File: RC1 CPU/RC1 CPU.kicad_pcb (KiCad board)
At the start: 2 copper layers, 99.1 x 99.1 mm, 43 parts, among them J1 Expansion, J2 RC1_UI_Port, J3 BARREL_JACK, M1 Mounting, M2 Mounting, M3 Mounting, M4 Mounting, U1 WD65C02, U2 HM62256BLP-7, U3 28C256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

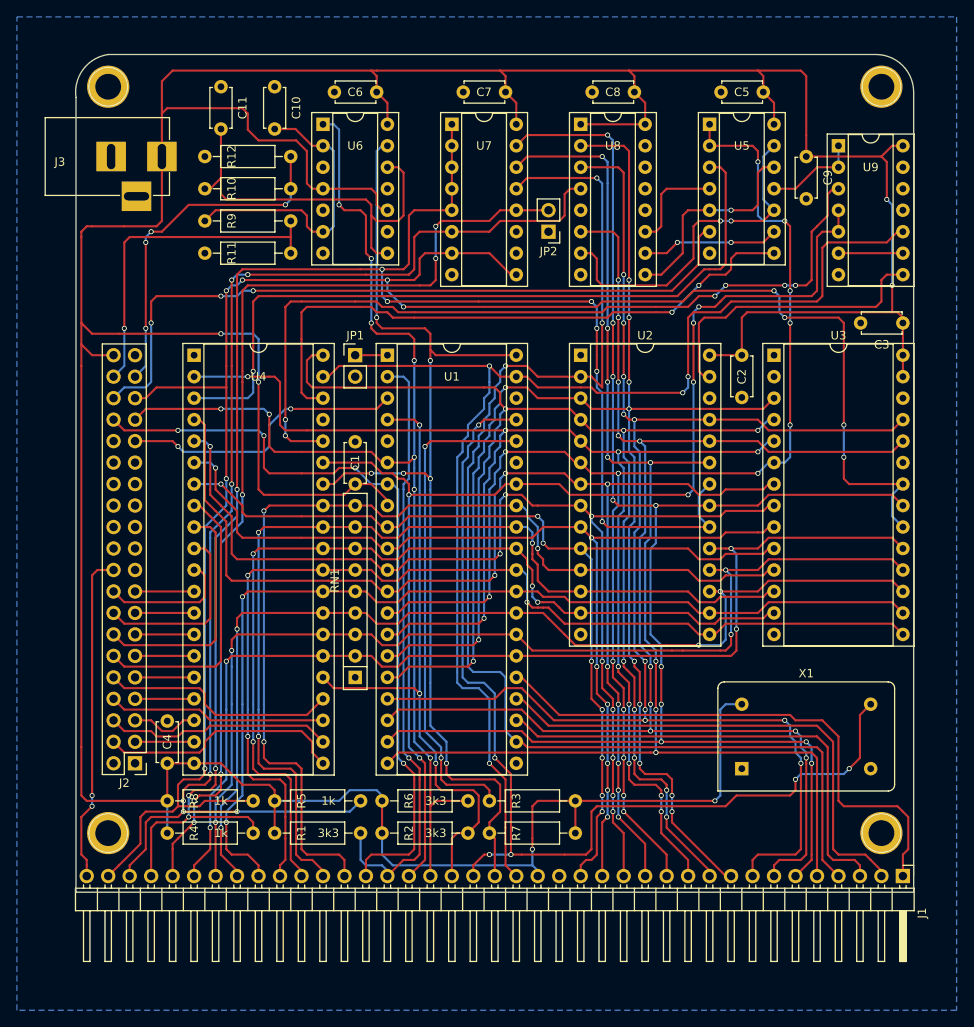
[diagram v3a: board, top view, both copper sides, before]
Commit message: Tweaked silkscreens and exported gerbers for CPU/UI
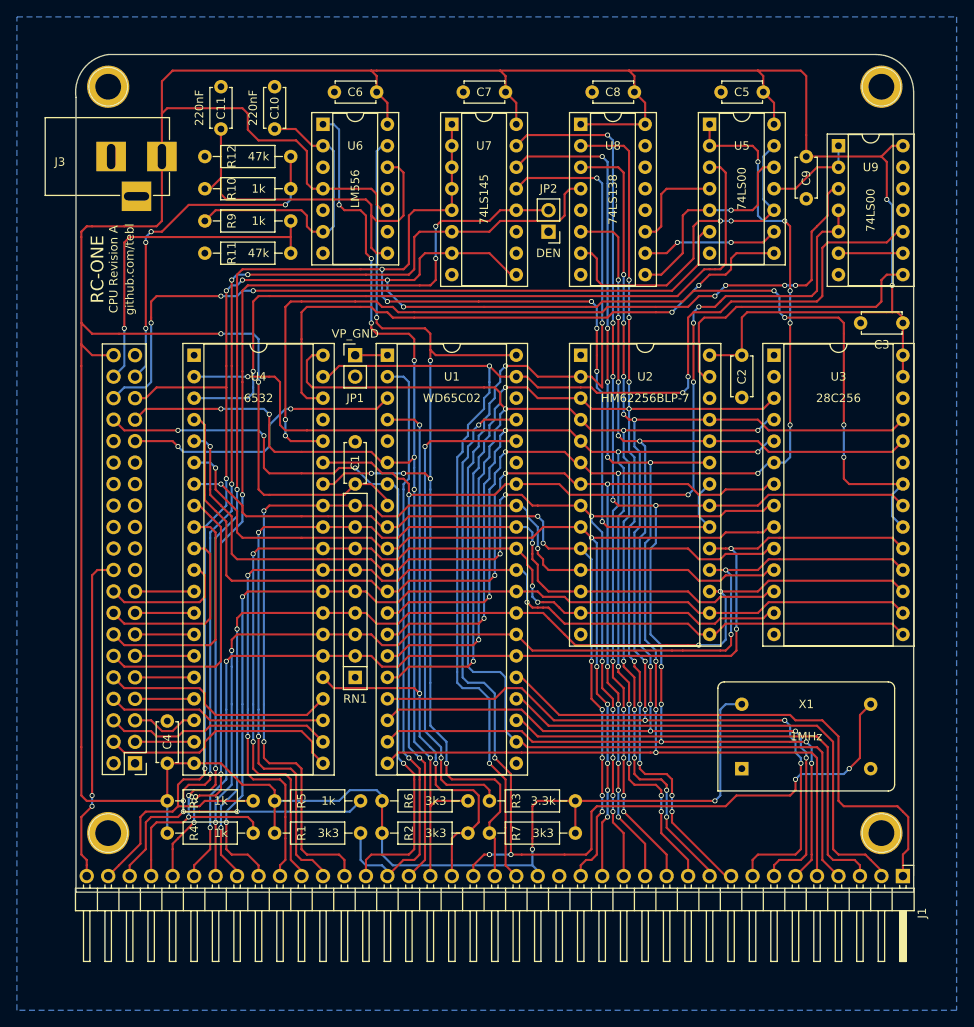
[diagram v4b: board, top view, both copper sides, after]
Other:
- board text added: "CPU Revision A"
- board text added: "RC-ONE"
- board text added: "github.com/tebl"
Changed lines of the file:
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@@
     (area 100.209871 48.184999 199.465001 147.395001)
     (thickness 1.6)
-    (drawings 6)
+    (drawings 9)
     (tracks 1946)
     (zones 0)
@@
     (descr "Through hole straight pin header, 2x20, 2.54mm pitch, double rows")
     (tags "Through hole pin header THT 2x20 2.54mm double row")
-    (fp_text reference J2 (at 1.27 -2.33 180) (layer F.SilkS)
-      (effects (font (size 1 1) (thickness 0.15)))
-    )
-    (fp_text value RC1_UI_Port (at 1.27 50.59 180) (layer F.Fab)
+    (fp_text reference J2 (at 1.27 -2.54 180) (layer F.Fab)
+      (effects (font (size 1 1) (thickness 0.15)))
+    )
+    (fp_text value RC1_UI_Port (at 1.27 50.8 180) (layer F.Fab)
       (effects (font (size 1 1) (thickness 0.15)))
     )
@@
     (descr "C, Disc series, Radial, pin pitch=5.00mm, , diameter*width=4.7*2.5mm^2, Capacitor, http://www.vishay.com/docs/45233/krseries.pdf")
     (tags "C Disc series Radial pin pitch 5.00mm  diameter 4.7mm width 2.5mm Capacitor")
-    (fp_text reference C9 (at 2.5 -2.56 270) (layer F.SilkS)
+    (fp_text reference C9 (at 2.54 0 270) (layer F.SilkS)
       (effects (font (size 1 1) (thickness 0.15)))
     )
@@
     (descr "C, Disc series, Radial, pin pitch=5.00mm, , diameter*width=4.7*2.5mm^2, Capacitor, http://www.vishay.com/docs/45233/krseries.pdf")
     (tags "C Disc series Radial pin pitch 5.00mm  diameter 4.7mm width 2.5mm Capacitor")
-    (fp_text reference C10 (at 2.5 -2.56 270) (layer F.SilkS)
-      (effects (font (size 1 1) (thickness 0.15)))
-    )
-    (fp_text value 220nF (at 2.5 2.56 270) (layer F.Fab)
+    (fp_text reference C10 (at 2.54 0 270) (layer F.SilkS)
+      (effects (font (size 1 1) (thickness 0.15)))
+    )
+    (fp_text value 220nF (at 2.5 2.56 270) (layer F.SilkS)
       (effects (font (size 1 1) (thickness 0.15)))
     )
@@
     (descr "C, Disc series, Radial, pin pitch=5.00mm, , diameter*width=4.7*2.5mm^2, Capacitor, http://www.vishay.com/docs/45233/krseries.pdf")
     (tags "C Disc series Radial pin pitch 5.00mm  diameter 4.7mm width 2.5mm Capacitor")
-    (fp_text reference C11 (at 2.5 -2.56 270) (layer F.SilkS)
-      (effects (font (size 1 1) (thickness 0.15)))
-    )
-    (fp_text value 220nF (at 2.5 2.56 270) (layer F.Fab)
+    (fp_text reference C11 (at 2.54 0 270) (layer F.SilkS)
+      (effects (font (size 1 1) (thickness 0.15)))
+    )
+    (fp_text value 220nF (at 2.5 2.56 270) (layer F.SilkS)
       (effects (font (size 1 1) (thickness 0.15)))
     )
@@
     (descr "Through hole straight pin header, 1x02, 2.54mm pitch, single row")
     (tags "Through hole pin header THT 1x02 2.54mm single row")
-    (fp_text reference JP1 (at 0 -2.33) (layer F.SilkS)
-      (effects (font (size 1 1) (thickness 0.15)))
-    )
-    (fp_text value VP_GND (at 0 4.87) (layer F.Fab)
+    (fp_text reference JP1 (at 0 5.08) (layer F.SilkS)
+      (effects (font (size 1 1) (thickness 0.15)))
+    )
+    (fp_text value VP_GND (at 0 -2.54) (layer F.SilkS)
       (effects (font (size 1 1) (thickness 0.15)))
     )
@@
     (descr "Through hole straight pin header, 1x02, 2.54mm pitch, single row")
     (tags "Through hole pin header THT 1x02 2.54mm single row")
-    (fp_text reference JP2 (at 0 -2.33 180) (layer F.SilkS)
-      (effects (font (size 1 1) (thickness 0.15)))
-    )
-    (fp_text value DEN (at 0 4.87 180) (layer F.Fab)
+    (fp_text reference JP2 (at 0 5.08 180) (layer F.SilkS)
+      (effects (font (size 1 1) (thickness 0.15)))
+    )
+    (fp_text value DEN (at 0 -2.54 180) (layer F.SilkS)
       (effects (font (size 1 1) (thickness 0.15)))
     )
@@
       (effects (font (size 1 1) (thickness 0.15)))
     )
-    (fp_text value 3.3k (at 6.35 0) (layer F.Fab)
+    (fp_text value 3.3k (at 6.35 0) (layer F.SilkS)
       (effects (font (size 1 1) (thickness 0.15)))
     )
@@
       (effects (font (size 1 1) (thickness 0.15)))
     )
-    (fp_text value 3k3 (at 6.35 0) (layer F.Fab)
+    (fp_text value 3k3 (at 6.35 0) (layer F.SilkS)
       (effects (font (size 1 1) (thickness 0.15)))
     )
@@
       (effects (font (size 1 1) (thickness 0.15)))
     )
-    (fp_text value 1k (at 6.35 0) (layer F.Fab)
+    (fp_text value 1k (at 6.35 0) (layer F.SilkS)
       (effects (font (size 1 1) (thickness 0.15)))
     )
@@
       (effects (font (size 1 1) (thickness 0.15)))
     )
-    (fp_text value 1k (at 6.35 0) (layer F.Fab)
+    (fp_text value 1k (at 6.35 0) (layer F.SilkS)
       (effects (font (size 1 1) (thickness 0.15)))
     )
@@
       (effects (font (size 1 1) (thickness 0.15)))
     )
-    (fp_text value 47k (at 6.35 0) (layer F.Fab)
+    (fp_text value 47k (at 6.35 0) (layer F.SilkS)
       (effects (font (size 1 1) (thickness 0.15)))
     )
@@
       (effects (font (size 1 1) (thickness 0.15)))
     )
-    (fp_text value 47k (at 6.35 0) (layer F.Fab)
+    (fp_text value 47k (at 6.35 0) (layer F.SilkS)
       (effects (font (size 1 1) (thickness 0.15)))
     )
@@
       (effects (font (size 1 1) (thickness 0.15)))
     )
-    (fp_text value WD65C02 (at 7.62 50.59) (layer F.Fab)
+    (fp_text value WD65C02 (at 7.62 5.08) (layer F.SilkS)
       (effects (font (size 1 1) (thickness 0.15)))
     )
@@
       (effects (font (size 1 1) (thickness 0.15)))
     )
-    (fp_text value 6532 (at 7.62 50.8) (layer F.Fab)
+    (fp_text value 6532 (at 7.62 5.08) (layer F.SilkS)
       (effects (font (size 1 1) (thickness 0.15)))
     )
@@
       (effects (font (size 1 1) (thickness 0.15)))
     )
-    (fp_text value 74LS00 (at 3.81 17.57) (layer F.Fab)
+    (fp_text value 74LS00 (at 3.81 7.62 90) (layer F.SilkS)
       (effects (font (size 1 1) (thickness 0.15)))
     )
@@
       (effects (font (size 1 1) (thickness 0.15)))
     )
-    (fp_text value LM556 (at 3.81 17.57) (layer F.Fab)
+    (fp_text value LM556 (at 3.81 7.62 90) (layer F.SilkS)
       (effects (font (size 1 1) (thickness 0.15)))
     )
@@
       (effects (font (size 1 1) (thickness 0.15)))
     )
-    (fp_text value 74LS145 (at 3.81 20.11) (layer F.Fab)
+    (fp_text value 74LS145 (at 3.81 8.89 90) (layer F.SilkS)
       (effects (font (size 1 1) (thickness 0.15)))
     )
@@
       (effects (font (size 1 1) (thickness 0.15)))
     )
-    (fp_text value 74LS138 (at 3.81 20.11) (layer F.Fab)
+    (fp_text value 74LS138 (at 3.81 8.89 90) (layer F.SilkS)
       (effects (font (size 1 1) (thickness 0.15)))
     )
@@
       (effects (font (size 1 1) (thickness 0.15)))
     )
-    (fp_text value 74LS00 (at 3.81 17.57) (layer F.Fab)
+    (fp_text value 74LS00 (at 3.81 7.62 90) (layer F.SilkS)
       (effects (font (size 1 1) (thickness 0.15)))
     )
@@
     (descr "Oscillator, DIP14, http://cdn-reichelt.de/documents/datenblatt/B400/OSZI.pdf")
     (tags oscillator)
-    (fp_text reference X1 (at 7.62 -11.26) (layer F.SilkS)
-      (effects (font (size 1 1) (thickness 0.15)))
-    )
-    (fp_text value 1MHz (at 7.62 3.74) (layer F.Fab)
-      (effects (font (size 1 1) (thickness 0.15)))
-    )
-    (fp_text user %R (at 7.62 -3.81) (layer F.Fab)
+    (fp_text reference X1 (at 7.62 -7.62) (layer F.SilkS)
+      (effects (font (size 1 1) (thickness 0.15)))
+    )
+    (fp_text value 1MHz (at 7.62 -3.81) (layer F.SilkS)
+      (effects (font (size 1 1) (thickness 0.15)))
+    )
+    (fp_text user %R (at 7.62 -7.62) (layer F.Fab)
       (effects (font (size 1 1) (thickness 0.15)))
     )
@@
     (descr "28-lead though-hole mounted DIP package, row spacing 15.24 mm (600 mils), Socket")
     (tags "THT DIP DIL PDIP 2.54mm 15.24mm 600mil Socket")
-    (fp_text reference U2 (at 7.62 -2.33) (layer F.SilkS)
-      (effects (font (size 1 1) (thickness 0.15)))
-    )
-    (fp_text value HM62256BLP-7 (at 7.62 35.35) (layer F.Fab)
+    (fp_text reference U2 (at 7.62 2.54) (layer F.SilkS)
+      (effects (font (size 1 1) (thickness 0.15)))
+    )
+    (fp_text value HM62256BLP-7 (at 7.62 5.08) (layer F.SilkS)
       (effects (font (size 1 1) (thickness 0.15)))
     )
@@
     (fp_line (start 16.8 34.65) (end 16.8 -1.6) (layer F.CrtYd) (width 0.05))
     (fp_line (start 16.8 -1.6) (end -1.55 -1.6) (layer F.CrtYd) (width 0.05))
-    (fp_text user %R (at 7.62 16.51) (layer F.Fab)
+    (fp_text user %R (at 7.62 2.54) (layer F.Fab)
       (effects (font (size 1 1) (thickness 0.15)))
     )
@@
     (descr "28-lead though-hole mounted DIP package, row spacing 15.24 mm (600 mils), Socket")
     (tags "THT DIP DIL PDIP 2.54mm 15.24mm 600mil Socket")
-    (fp_text reference U3 (at 7.62 -2.33) (layer F.SilkS)
-      (effects (font (size 1 1) (thickness 0.15)))
-    )
-    (fp_text value 28C256 (at 7.62 35.35) (layer F.Fab)
+    (fp_text reference U3 (at 7.62 2.54) (layer F.SilkS)
+      (effects (font (size 1 1) (thickness 0.15)))
+    )
+    (fp_text value 28C256 (at 7.62 5.08) (layer F.SilkS)
       (effects (font (size 1 1) (thickness 0.15)))
     )
@@
     (fp_line (start 16.8 34.65) (end 16.8 -1.6) (layer F.CrtYd) (width 0.05))
     (fp_line (start 16.8 -1.6) (end -1.55 -1.6) (layer F.CrtYd) (width 0.05))
-    (fp_text user %R (at 7.62 16.51) (layer F.Fab)
+    (fp_text user %R (at 7.62 2.54) (layer F.Fab)
       (effects (font (size 1 1) (thickness 0.15)))
     )
@@
     (descr "9-pin Resistor SIP pack")
     (tags R)
-    (fp_text reference RN1 (at 11.43 -2.4 90) (layer F.SilkS)
+    (fp_text reference RN1 (at -2.54 0 180) (layer F.SilkS)
       (effects (font (size 1 1) (thickness 0.15)))
     )
@@
     )
   )
+  (gr_text github.com/tebl (at 106.68 73.66 90) (layer F.SilkS)
+    (effects (font (size 1 1) (thickness 0.15)))
+  )
+  (gr_text "CPU Revision A" (at 104.775 73.66 90) (layer F.SilkS)
+    (effects (font (size 1 1) (thickness 0.15)))
+  )
+  (gr_text RC-ONE (at 102.87 73.66 90) (layer F.SilkS)
+    (effects (font (size 1.5 1.5) (thickness 0.3)))
+  )
   (gr_line (start 104.14 48.26) (end 194.945 48.26) (angle 90) (layer Edge.Cuts) (width 0.15))

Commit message: Added ability to override K0/K7
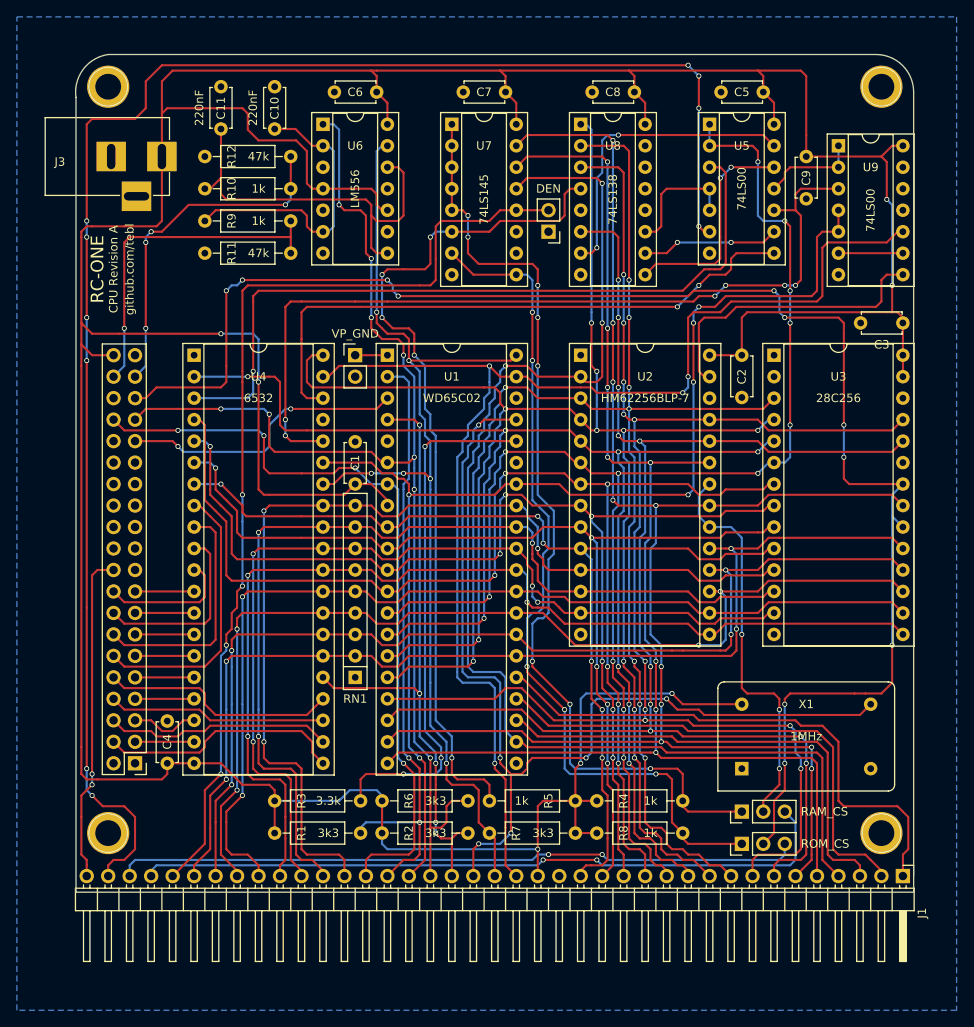
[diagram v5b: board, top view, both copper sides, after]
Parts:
- added JP3: RAM_CS, Pin_Headers:Pin_Header_Straight_1x03_Pitch2.54mm, F.Cu at (179.1, 137.8)
- added JP4: ROM_CS, Pin_Headers:Pin_Header_Straight_1x03_Pitch2.54mm, F.Cu at (179.1, 141.6)
- moved R4 50.9 mm to (161.9, 136.5)
- moved R8 50.9 mm to (161.9, 140.3)
- moved R5 35.6 mm to (159.4, 136.5), turned to 180 degrees
- moved R3 15.2 mm to (134.0, 136.5), turned to 180 degrees
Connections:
- J1 pad 36: K0 -> K0_EXT
- J1 pad 37: K5 -> K7_EXT
- J1 pad 38: K7 -> IO3
- J2 pad 36: IO3 -> (no net)
- R4 pad 2: K0 -> Net-(JP3-Pad1)
- R8 pad 2: K7 -> Net-(JP4-Pad1)
- U5 pad 10: Net-(U5-Pad10) -> RAM_SEL
- U5 pad 13: Net-(U5-Pad10) -> Net-(U5-Pad13)
- U5 pad 5: Net-(U5-Pad12) -> Net-(U5-Pad4)
- U7 pad 1: K0 -> Net-(JP3-Pad1)
- U7 pad 2: K0 -> Net-(JP3-Pad1)
- U7 pad 3: K0 -> Net-(JP3-Pad1)
- U7 pad 4: K0 -> Net-(JP3-Pad1)
- U7 pad 5: K0 -> Net-(JP3-Pad1)
- U7 pad 7: K7 -> Net-(JP4-Pad1)
- U7 pad 9: K7 -> Net-(JP4-Pad1)
- U8 pad 1: VCC -> /A6
- U8 pad 7: Net-(U5-Pad10) -> Net-(U5-Pad13)
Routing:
- net K0: track 203.4 -> 47.3 mm, vias 10 -> 3
- net Net-(JP3-Pad1): track 0.00 -> 113.2 mm, vias 0 -> 8
- net IO3: track 86.1 -> 192.4 mm, vias 3 -> 10
- net Net-(JP4-Pad1): track 0.00 -> 101.3 mm, vias 0 -> 6
- net K0_EXT: track 0.00 -> 84.1 mm, vias 0 -> 2
- net K7_EXT: track 0.00 -> 81.1 mm, vias 0 -> 2
- net K5: track 149.4 -> 101.5 mm, vias 7 -> 5
- net K7: track 230.0 -> 183.8 mm, vias 10 -> 11
- net Net-(U5-Pad10): track 40.5 -> 0.00 mm, vias 2 -> 0
- net /A6: track 162.7 -> 200.8 mm, vias 9 -> 10
- net Net-(U5-Pad13): track 0.00 -> 36.2 mm, vias 0 -> 2
- net VCC: track 503.6 -> 491.8 mm, vias 6 -> 7
- net /PHI0: track 122.3 -> 117.7 mm
- net RAM_SEL: track 97.0 -> 101.2 mm
- net /BE: track 58.7 -> 62.5 mm, vias 2 -> 3
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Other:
- board text added: "RAM_CS"
- board text added: "ROM_CS"

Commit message: Added RAM A13/A14 reconnects for external RAM logic
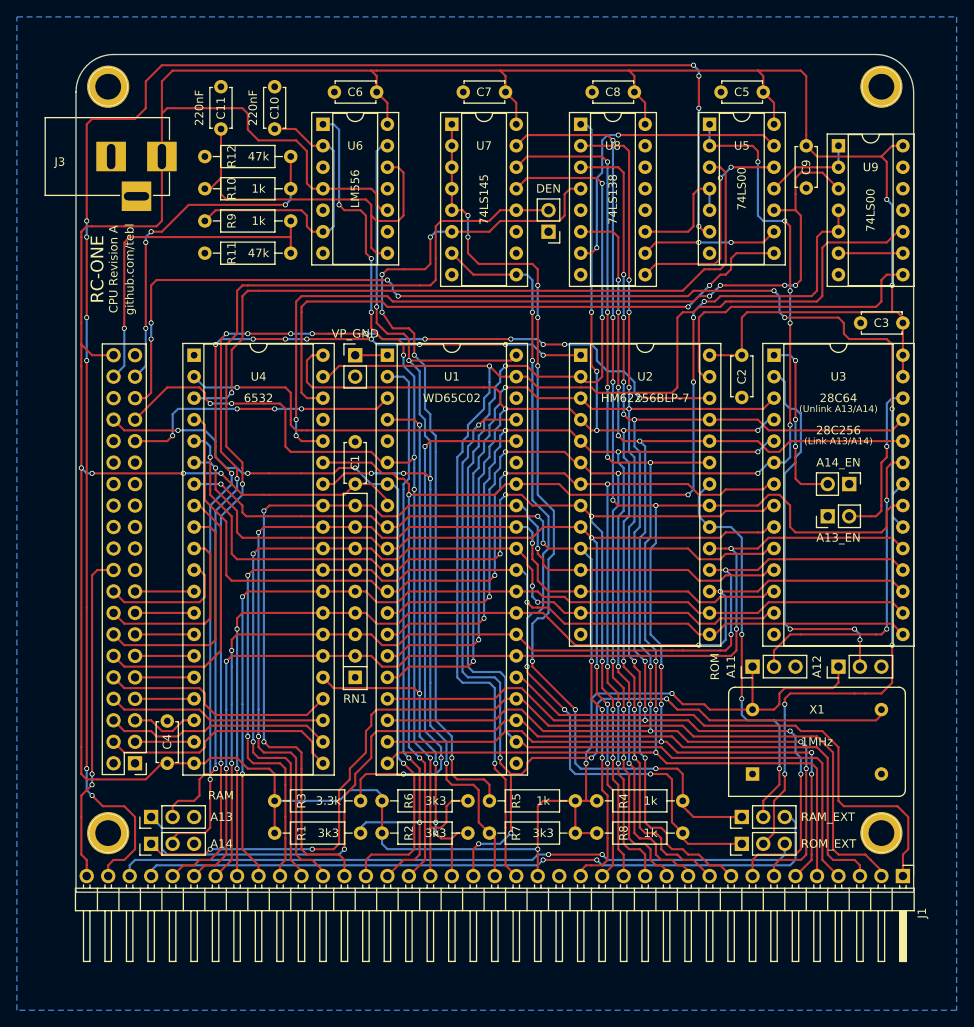
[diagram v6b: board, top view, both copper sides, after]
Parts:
- added JP10: A14, Pin_Headers:Pin_Header_Straight_1x03_Pitch2.54mm, F.Cu at (109.2, 141.6)
- added JP5: A13_EN, Pin_Headers:Pin_Header_Straight_1x02_Pitch2.54mm, F.Cu at (189.2, 102.9)
- added JP6: A14_EN, Pin_Headers:Pin_Header_Straight_1x02_Pitch2.54mm, F.Cu at (191.8, 99.1)
- added JP7: A11, Pin_Headers:Pin_Header_Straight_1x03_Pitch2.54mm, F.Cu at (180.3, 120.7)
- added JP8: A12, Pin_Headers:Pin_Header_Straight_1x03_Pitch2.54mm, F.Cu at (190.5, 120.7)
- added JP9: A13, Pin_Headers:Pin_Header_Straight_1x03_Pitch2.54mm, F.Cu at (109.2, 138.4)
- moved X1 1.42 mm to (180.3, 133.3)
- moved C9 1.27 mm to (186.7, 59.1)
- moved JP3 0.64 mm to (179.1, 138.4)
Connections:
- U2 pad 1: GND -> /A14_RAM
- U2 pad 26: GND -> /A13_RAM
- U3 pad 1: GND -> Net-(JP6-Pad2)
- U3 pad 2: GND -> /A12_W
- U3 pad 23: GND -> /A11_W
- U3 pad 26: GND -> Net-(JP5-Pad2)
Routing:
- net /A13_RAM: track 0.00 -> 125.3 mm, vias 0 -> 12
- net /A14_RAM: track 0.00 -> 108.8 mm, vias 0 -> 10
- net /A13: track 56.1 -> 114.7 mm, vias 0 -> 1
- net /A14: track 59.3 -> 117.0 mm, vias 0 -> 2
- net /A12_W: track 0.00 -> 45.3 mm, vias 0 -> 3
- net /A11_W: track 0.00 -> 38.1 mm, vias 0 -> 2
- net Net-(JP6-Pad2): track 0.00 -> 20.8 mm, vias 0 -> 3
- net Net-(JP5-Pad2): track 0.00 -> 19.8 mm, vias 0 -> 1
- net /A10: track 187.2 -> 192.1 mm
- net /DEN: track 116.5 -> 119.9 mm, vias 4 -> 2
- net /~NMI: track 142.7 -> 145.5 mm
- net VCC: track 491.8 -> 494.5 mm, vias 7 -> 9
- net /D4: track 118.7 -> 116.0 mm
- net /PHI0: track 117.7 -> 119.6 mm
- net /SYNC: track 91.3 -> 90.2 mm
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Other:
- outline, holes or cut-outs redrawn
- board text added: "(Link A13/A14)"
- board text added: "(Unlink A13/A14)"
- board text added: "28C64"
- board text added: "A13"
- board text added: "A14"
- board text added: "RAM"
- board text added: "RAM_EXT"
- board text added: "ROM"
- board text added: "ROM_EXT"
- board text removed: "RAM_CS"
- board text removed: "ROM_CS"
